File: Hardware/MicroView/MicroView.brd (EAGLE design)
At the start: 20.5 x 20.5 mm, 23 parts, among them J1 OLED_SCREEN, J2 MICROVIEW-16, J3 M03NS_SLIM, U1 MIC5205 3.3V, U2 SPX3819M5-L-5-0, U3 ATMEGA328P, Y1 16MHz

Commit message: Adding fids to both boards
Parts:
- added FID1, FID3: FIDUCIAL1X2, SparkFun-Aesthetics:FIDUCIAL-1X2
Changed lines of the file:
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@@
 <element name="LOGO1" library="SparkFun-Aesthetics" package="OSHW-LOGO-S" value="OSHW-LOGOS" x="-4.191" y="4.191"/>
 <element name="LOGO4" library="SparkFun-Aesthetics" package="SFE_LOGO_NAME_FLAME_.1" value="SFE_LOGO_NAME_FLAME.1_INCH" x="-8.128" y="0"/>
+<element name="FID1" library="SparkFun-Aesthetics" package="FIDUCIAL-1X2" value="FIDUCIAL1X2" x="7.62" y="9.525" rot="MR0"/>
+<element name="FID3" library="SparkFun-Aesthetics" package="FIDUCIAL-1X2" value="FIDUCIAL1X2" x="-5.08" y="-9.525" rot="MR0"/>
 </elements>
 <signals>

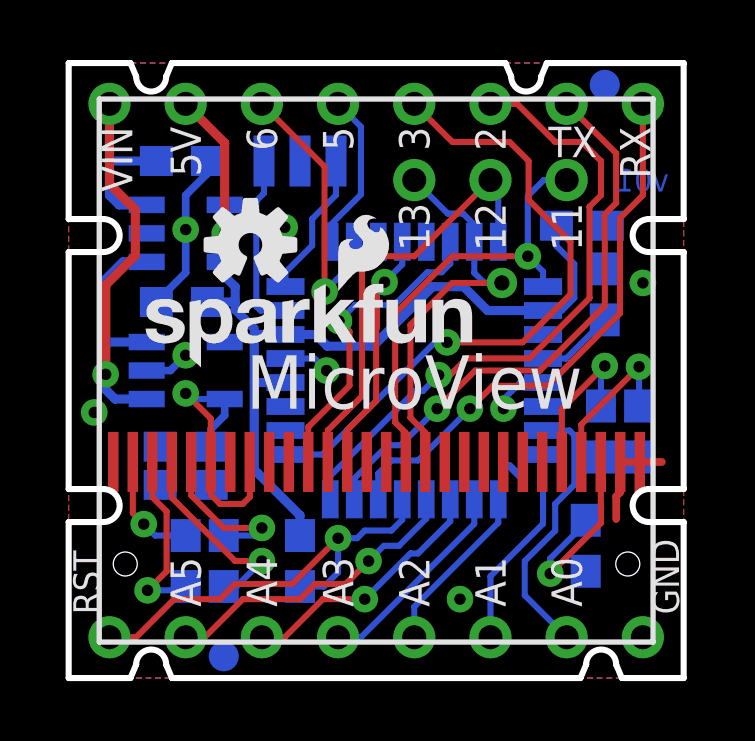
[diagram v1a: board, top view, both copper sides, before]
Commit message: Staggering/increasing drill on headers
Also spacing out resistors, increasing header fp on MicroViewUSB.
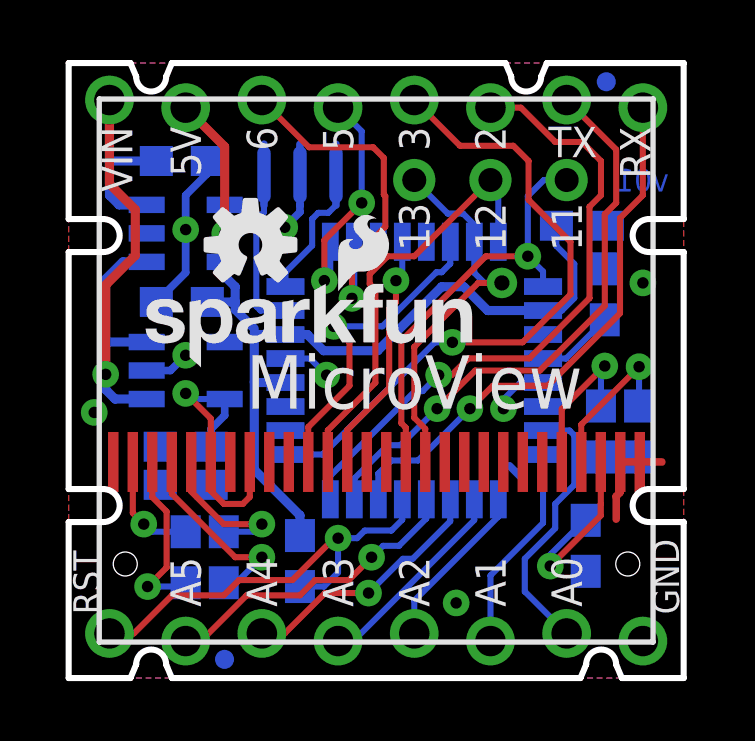
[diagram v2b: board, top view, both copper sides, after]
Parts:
- FID1, FID3: value FIDUCIAL1X2 -> FIDUCIALUFIDUCIAL; device SparkFun-Aesthetics:FIDUCIAL-1X2 -> SparkFun-Aesthetics:MICRO-FIDUCIAL
- moved Y1 0.46 mm to (-2.54, 6.53)
- moved C5 0.13 mm to (-6.35, -6.22)
- moved C6 0.13 mm to (-5.08, -6.22)
- moved FID1 0.11 mm to (7.67, 9.63)
- moved FID3 0.10 mm to (-5.05, -9.63)
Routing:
- net D6: track 9.19 -> 11.9 mm
- net D5: track 5.34 -> 7.98 mm, vias 0 -> 2
- net N$8: track 5.98 -> 4.51 mm
- net GND: track 14.4 -> 15.4 mm
- net D13/SCK: track 15.1 -> 14.2 mm
- net D11/MOSI: track 13.7 -> 13.1 mm

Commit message: Microview v02 -- new resistors and 3.3Vreg change
* Added pull-down resistor to OLED Reset. Also moved that pin to D7 on
the Arduino.
* Added pull-up resistor to D10/SS.
* Moved 3.3V regulator input to the 5V line (from Vin)
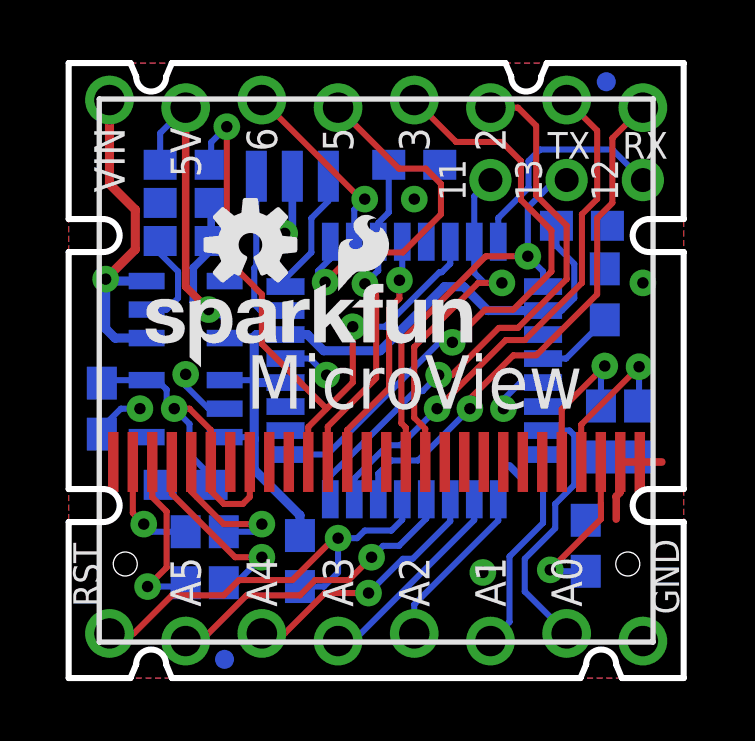
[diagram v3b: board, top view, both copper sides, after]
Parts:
- removed J3: M03NS_SLIM, microView-temp:1X03_NS_SLIM
- removed Y1: 16MHz, SparkFun-FreqCtrl:RESONATOR-SMD
- added J4: M03NS_SLIM, microView-temp:1X03_NS_SLIM
- added R3, R4: 10K, SparkFun-Resistors:0603-RES
- added Y2: RESONATORSMD, microView-temp:RESONATOR-SMD
- moved C2 3.78 mm to (-9.14, -1.27), turned to 270 degrees
- moved U2 2.54 mm to (-6.35, 2.03)
- moved C4 2.04 mm to (-6.35, 4.32)
- moved C1 1.40 mm to (-6.35, 5.59), turned to 0 degrees
- moved C3 1.27 mm to (-6.35, -3.81)
- moved U1 1.27 mm to (-6.35, -1.27), turned to 270 degrees
- turned C10 to 90 degrees
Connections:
- new net D7/!RESET!: OLED1.12, R4.2, U3.11
- net 5V: now also C1.1, R3.2, U1.1, U1.3
- net D10/SS: now also R3.1
- net D11/MOSI: now also J4.1; no longer J3.1
- net D12/MISO: now also J4.3; no longer J3.2, OLED1.12
- net D13/SCK: now also J4.2; no longer J3.3
- net GND: now also R4.1, Y2.2; no longer Y1.2
- net N$8: now also Y2.1; no longer Y1.1
- net N$9: now also Y2.3; no longer Y1.3
- net VIN: no longer C1.1, U1.1, U1.3
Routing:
- net VIN: track 25.6 -> 12.7 mm
- net D10/SS: track 10.8 -> 22.3 mm, vias 1 -> 2
- net D7/!RESET!: track 0.00 -> 11.1 mm, vias 0 -> 1
- net 5V: track 32.8 -> 41.1 mm
- net D12/MISO: track 14.5 -> 7.50 mm
- net D6: track 11.9 -> 6.36 mm
- net D5: track 7.98 -> 11.9 mm, vias 2 -> 1
- net D2: track 21.0 -> 18.7 mm
- net 3.3V: track 10.8 -> 12.4 mm
- net D3: track 21.4 -> 19.9 mm
- net TXD: track 19.1 -> 17.7 mm
- net N$8: track 4.51 -> 5.42 mm
- net D11/MOSI: track 13.1 -> 12.2 mm
- net GND: track 15.4 -> 16.2 mm
- net N$1: track 6.27 -> 5.50 mm
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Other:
- board text removed: "v01"

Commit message: Tying 3.3V reg enable to an ATmega pin (D4)
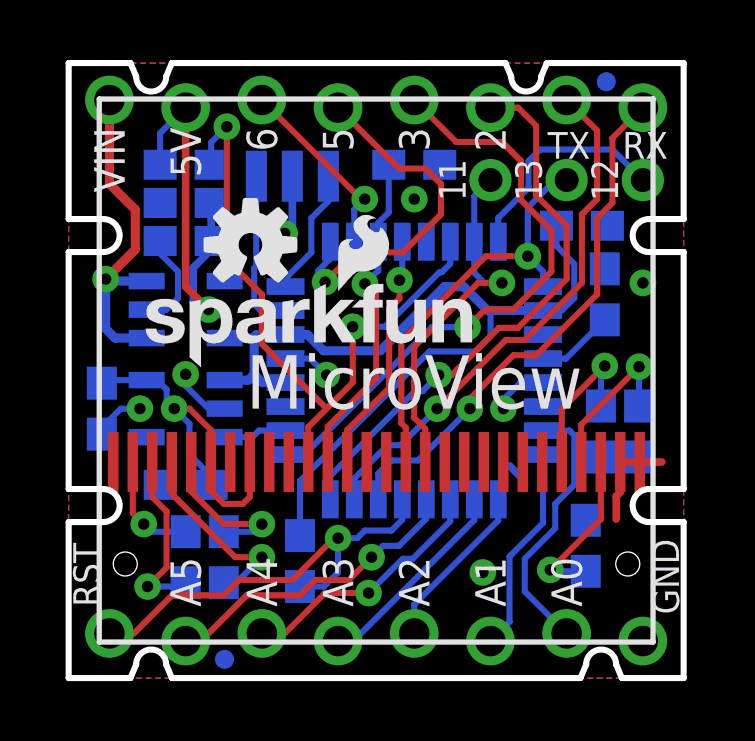
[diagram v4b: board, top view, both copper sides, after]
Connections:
- new net D4/3.3V_EN: U1.3, U3.2
- net 5V: no longer U1.3
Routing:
- net 5V: track 41.1 -> 45.3 mm
- net D4/3.3V_EN: track 0.00 -> 2.12 mm
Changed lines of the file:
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@@
 <layer number="50" name="dxf" color="7" fill="1" visible="no" active="no"/>
 <layer number="51" name="tDocu" color="6" fill="1" visible="yes" active="yes"/>
-<layer number="52" name="bDocu" color="7" fill="1" visible="yes" active="yes"/>
+<layer number="52" name="bDocu" color="7" fill="1" visible="no" active="yes"/>
 <layer number="53" name="tGND_GNDA" color="7" fill="9" visible="no" active="no"/>
 <layer number="54" name="bGND_GNDA" color="1" fill="9" visible="no" active="no"/>
@@
 <wire x1="5.5626" y1="2" x2="6.191" y2="2" width="0.2032" layer="16"/>
 <wire x1="6.191" y1="2" x2="6.604" y2="2.413" width="0.2032" layer="16"/>
-<wire x1="-2.54" y1="-5.5" x2="-2.54" y2="-4.826" width="0.3048" layer="16"/>
-<wire x1="-2.54" y1="-4.826" x2="-4.064" y2="-3.302" width="0.3048" layer="16"/>
-<wire x1="-4.064" y1="-3.302" x2="-4.064" y2="-2.286" width="0.3048" layer="16"/>
-<wire x1="-4.064" y1="-2.286" x2="-4.064" y2="-0.381" width="0.3048" layer="16"/>
 <wire x1="5.5626" y1="2" x2="3.715" y2="2" width="0.3048" layer="16"/>
 <wire x1="3.715" y1="2" x2="2.921" y2="2.794" width="0.3048" layer="16"/>
 <wire x1="-3.0226" y1="1.2" x2="-3.994" y2="1.2" width="0.3048" layer="16"/>
-<wire x1="-3.0226" y1="-0.4" x2="-4.045" y2="-0.4" width="0.3048" layer="16"/>
-<wire x1="-4.045" y1="-0.4" x2="-4.064" y2="-0.381" width="0.254" layer="16"/>
 <wire x1="2.921" y1="2.794" x2="2.2733" y2="2.794" width="0.3048" layer="16"/>
 <wire x1="-3.0226" y1="1.2" x2="-2.2922" y2="1.2" width="0.3048" layer="16"/>
@@
 <contactref element="U1" pad="1"/>
 <contactref element="C1" pad="1"/>
-<contactref element="U1" pad="3"/>
-<wire x1="-5.0499" y1="-0.32" x2="-4.125" y2="-0.32" width="0.2032" layer="16"/>
-<wire x1="-5.0499" y1="-2.22" x2="-4.13" y2="-2.22" width="0.2032" layer="16"/>
-<wire x1="-4.13" y1="-2.22" x2="-4.064" y2="-2.286" width="0.2032" layer="16"/>
 <wire x1="-5.0499" y1="1.082" x2="-4.112" y2="1.082" width="0.3048" layer="16"/>
 <wire x1="-4.112" y1="1.082" x2="-3.994" y2="1.2" width="0.3048" layer="16"/>
-<wire x1="-4.064" y1="-0.381" x2="-4.064" y2="1.034" width="0.3048" layer="16"/>
 <wire x1="-4.064" y1="1.034" x2="-4.112" y2="1.082" width="0.3048" layer="16"/>
-<wire x1="-4.064" y1="-0.381" x2="-4.125" y2="-0.32" width="0.254" layer="16"/>
 <wire x1="-5.5" y1="4.318" x2="-5.5" y2="4.025" width="0.254" layer="16"/>
 <wire x1="-5.5" y1="4.025" x2="-6.096" y2="3.429" width="0.254" layer="16"/>
@@
 <wire x1="-7.2" y1="6.858" x2="-7.2" y2="7.913" width="0.2032" layer="16"/>
 <wire x1="-7.2" y1="7.913" x2="-6.35" y2="8.763" width="0.2032" layer="16"/>
+<wire x1="-2.54" y1="-5.5" x2="-2.54" y2="-3.683" width="0.2032" layer="16"/>
+<wire x1="-2.54" y1="-3.683" x2="1.778" y2="0.635" width="0.2032" layer="16"/>
+<wire x1="1.778" y1="0.635" x2="3.302" y2="0.635" width="0.2032" layer="16"/>
+<wire x1="3.302" y1="0.635" x2="3.81" y2="1.143" width="0.2032" layer="16"/>
+<wire x1="3.81" y1="1.143" x2="3.81" y2="1.905" width="0.2032" layer="16"/>
+<wire x1="3.81" y1="1.905" x2="3.715" y2="2" width="0.2032" layer="16"/>
+<wire x1="-4.064" y1="1.034" x2="-4.064" y2="-0.127" width="0.3048" layer="16"/>
+<wire x1="-4.064" y1="-0.127" x2="-4.257" y2="-0.32" width="0.3048" layer="16"/>
+<wire x1="-5.0499" y1="-0.32" x2="-4.257" y2="-0.32" width="0.3048" layer="16"/>
+<wire x1="-3.0226" y1="-0.4" x2="-3.791" y2="-0.4" width="0.3048" layer="16"/>
+<wire x1="-3.791" y1="-0.4" x2="-4.064" y2="-0.127" width="0.3048" layer="16"/>
 </signal>
 <signal name="N$1">
@@
 <contactref element="U3" pad="1"/>
 <contactref element="J2" pad="12"/>
-<via x="2.54" y="0.9398" extent="1-16" drill="0.381"/>
+<via x="3.048" y="1.4478" extent="1-16" drill="0.381"/>
 <wire x1="4.826" y1="5.6896" x2="4.826" y2="6.985" width="0.2032" layer="1"/>
 <wire x1="4.826" y1="6.985" x2="4.191" y2="7.62" width="0.2032" layer="1"/>
 <wire x1="4.191" y1="7.62" x2="2.667" y2="7.62" width="0.2032" layer="1"/>
 <wire x1="2.667" y1="7.62" x2="1.27" y2="9.017" width="0.2032" layer="1"/>
-<wire x1="-3.0226" y1="-2.8" x2="-1.6316" y2="-2.8" width="0.2032" layer="16"/>
-<wire x1="-1.6316" y1="-2.8" x2="2.1082" y2="0.9398" width="0.2032" layer="16"/>
-<wire x1="2.54" y1="0.9398" x2="2.1082" y2="0.9398" width="0.2032" layer="16"/>
-<wire x1="2.54" y1="0.9398" x2="3.6322" y2="2.032" width="0.2032" layer="1"/>
+<wire x1="-3.0226" y1="-2.8" x2="-2.3936" y2="-2.8" width="0.2032" layer="16"/>
+<wire x1="-2.3936" y1="-2.8" x2="1.8542" y2="1.4478" width="0.2032" layer="16"/>
+<wire x1="3.048" y1="1.4478" x2="1.8542" y2="1.4478" width="0.2032" layer="16"/>
+<wire x1="3.048" y1="1.4478" x2="3.6322" y2="2.032" width="0.2032" layer="1"/>
 <wire x1="3.6322" y1="2.032" x2="4.572" y2="2.032" width="0.2032" layer="1"/>
 <wire x1="4.572" y1="2.032" x2="5.842" y2="3.302" width="0.2032" layer="1"/>
@@
 <wire x1="0.42" y1="6.858" x2="0.42" y2="5.2714" width="0.2032" layer="16"/>
 </signal>
+<signal name="D4/3.3V_EN">
+<contactref element="U1" pad="3"/>
+<contactref element="U3" pad="2"/>
+<wire x1="-3.0226" y1="-2" x2="-3.905" y2="-2" width="0.2032" layer="16"/>
+<wire x1="-3.905" y1="-2" x2="-4.125" y2="-2.22" width="0.2032" layer="16"/>
+<wire x1="-5.0499" y1="-2.22" x2="-4.125" y2="-2.22" width="0.2032" layer="16"/>
+</signal>
 </signals>

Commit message: Series resistors on MOSI and SCK (v03)
Limits current into OLED I/O lines. This in conjunction with some code
changes will help to protect the display from overvoltage.

This required removing pull-down resistor to RESET and pull-up to SS.
BUT! You can still program the display, using an ICSP, with the series
resistors on MOSI and SCK.
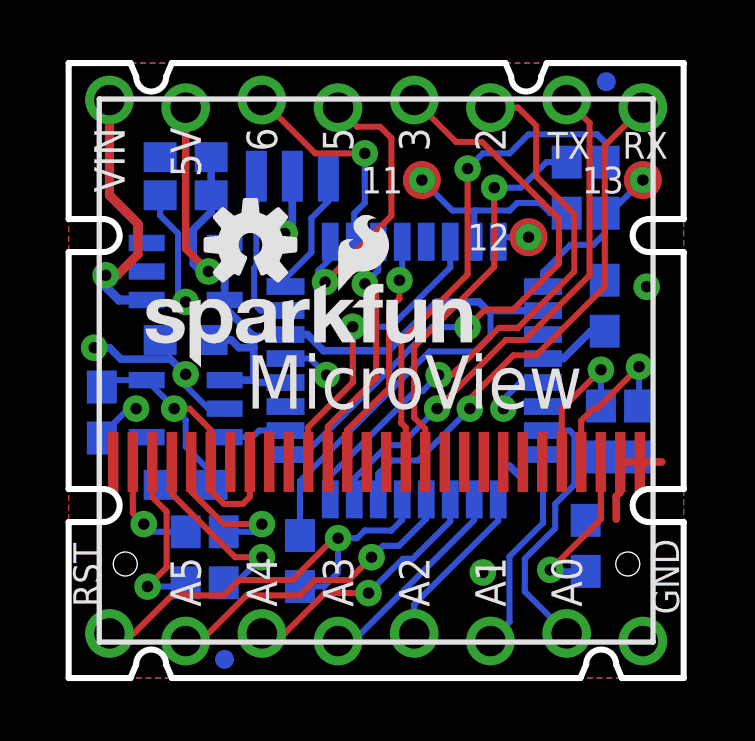
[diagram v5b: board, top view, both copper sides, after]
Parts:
- removed J4: M03NS_SLIM, microView-temp:1X03_NS_SLIM
- added TP1, TP2, TP3: (no value), SparkFun-Passives:PAD.03X.05
- R3, R4: value 10K -> 1k
- Y2: value RESONATORSMD -> 16MHz
- moved R3 14.0 mm to (7.62, 6.10), turned to 270 degrees
- moved C7 13.4 mm to (-6.35, 7.11), turned to 0 degrees
- moved R4 5.14 mm to (6.35, 6.10), turned to 270 degrees
- moved C1 4.57 mm to (-6.35, 1.02)
- moved C4 1.52 mm to (-6.35, 5.84)
- moved U2 1.27 mm to (-6.35, 3.30)
- moved C8 0.38 mm to (7.62, 2.16)
- moved C2 0.13 mm to (-9.14, -1.40)
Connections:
- new net D11: R4.2, TP3.P$1, U3.15
- new net D13: R3.2, TP2.P$1, U3.17
- net 5V: no longer R3.2
- net D10/SS: no longer R3.1
- net D11/MOSI: now also R4.1; no longer J4.1, U3.15
- net D12/MISO: now also TP1.P$1; no longer J4.3
- net D13/SCK: now also R3.1; no longer J4.2, U3.17
- net D7/!RESET!: no longer R4.2
- net GND: no longer R4.1
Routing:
- net D10/SS: track 22.3 -> 10.1 mm, vias 2 -> 1
- net D11: track 0.00 -> 6.55 mm, vias 0 -> 1
- net D12/MISO: track 7.50 -> 1.07 mm, vias 0 -> 1
- net D13: track 0.00 -> 5.47 mm, vias 0 -> 1
- net 5V: track 45.3 -> 39.9 mm
- net GND: track 16.2 -> 19.8 mm, vias 8 -> 9
- net D7/!RESET!: track 11.1 -> 8.35 mm
- net D13/SCK: track 14.0 -> 16.6 mm
- net D5: track 11.9 -> 9.52 mm
- net VIN: track 12.7 -> 14.3 mm
- net D11/MOSI: track 12.2 -> 13.2 mm
- net D6: track 6.36 -> 7.26 mm
- net C2N: track 5.94 -> 6.64 mm

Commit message: Moving some silk around. Production boards (v10).
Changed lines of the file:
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@@
 <plain>
 <text x="9.652" y="-8.128" size="0.889" layer="22" font="vector" ratio="15" rot="MR270" align="center-right">GND</text>
-<text x="5.842" y="-7.874" size="1.016" layer="22" font="vector" ratio="15" rot="MR270" align="center-right">A0</text>
+<text x="5.461" y="-7.366" size="1.016" layer="22" font="vector" ratio="15" rot="MR180" align="center">A0</text>
 <text x="3.81" y="-7.874" size="1.016" layer="22" font="vector" ratio="15" rot="MR270" align="center-right">A1</text>
 <text x="1.27" y="-7.874" size="1.016" layer="22" font="vector" ratio="15" rot="MR270" align="center-right">A2</text>
 <text x="-1.27" y="-7.874" size="1.016" layer="22" font="vector" ratio="15" rot="MR270" align="center-right">A3</text>
-<text x="-3.81" y="-7.874" size="1.016" layer="22" font="vector" ratio="15" rot="MR270" align="center-right">A4</text>
 <text x="-6.35" y="-7.874" size="1.016" layer="21" font="vector" ratio="15" rot="R270" align="center-right">A5</text>
-<text x="-9.652" y="-7.874" size="0.889" layer="22" font="vector" ratio="15" rot="MR270" align="center-right">RST</text>
-<text x="8.7884" y="7.9502" size="0.889" layer="22" font="vector" ratio="15" rot="MR0" align="top-center">RX</text>
-<text x="6.2484" y="7.9502" size="0.889" layer="22" font="vector" ratio="15" rot="MR0" align="top-center">TX</text>
-<text x="3.81" y="8.0264" size="0.889" layer="22" font="vector" ratio="15" rot="MR90" align="center-right">2</text>
-<text x="1.27" y="8.255" size="0.889" layer="22" font="vector" ratio="15" rot="MR90" align="center-right">3</text>
+<text x="-9.525" y="-7.874" size="0.889" layer="22" font="vector" ratio="15" rot="MR270" align="center-right">RST</text>
+<text x="8.7884" y="7.8232" size="0.889" layer="22" font="vector" ratio="15" rot="MR0" align="top-center">RX</text>
+<text x="3.81" y="8.001" size="0.889" layer="22" font="vector" ratio="15" rot="MR90" align="center-right">2</text>
+<text x="1.27" y="8.001" size="0.889" layer="22" font="vector" ratio="15" rot="MR90" align="center-right">3</text>
 <text x="-3.81" y="8.1026" size="1.016" layer="21" font="vector" ratio="15" rot="R270" align="center-left">6</text>
 <text x="-6.35" y="8.1026" size="1.016" layer="21" font="vector" ratio="15" rot="R270" align="center-left">5V</text>
-<text x="-8.89" y="8.255" size="0.889" layer="22" font="vector" ratio="15" rot="MR270" align="center-left">VIN</text>
-<text x="8.9662" y="7.9502" size="0.889" layer="21" font="vector" ratio="15" align="top-center">RX</text>
+<text x="-8.89" y="8.001" size="0.889" layer="22" font="vector" ratio="15" rot="MR270" align="center-left">VIN</text>
+<text x="8.4582" y="7.9502" size="0.889" layer="21" font="vector" ratio="15" align="top-center">RX</text>
 <text x="6.4262" y="7.9502" size="0.889" layer="21" font="vector" ratio="15" align="top-center">TX</text>
 <text x="3.81" y="8.1026" size="1.016" layer="21" font="vector" ratio="15" rot="R90" align="center-right">2</text>
 <text x="1.27" y="8.1026" size="1.016" layer="21" font="vector" ratio="15" rot="R90" align="center-right">3</text>
 <text x="-1.27" y="8.1026" size="1.016" layer="21" font="vector" ratio="15" rot="R90" align="center-right">5</text>
-<text x="-8.89" y="8.1026" size="1.016" layer="21" font="vector" ratio="15" rot="R90" align="center-right">VIN</text>
+<text x="-8.509" y="8.1026" size="1.016" layer="21" font="vector" ratio="15" rot="R90" align="center-right">VIN</text>
 <text x="9.652" y="-8.128" size="0.889" layer="21" font="vector" ratio="15" rot="R90" align="center-left">GND</text>
-<text x="6.35" y="-7.874" size="1.016" layer="21" font="vector" ratio="15" rot="R90" align="center-left">A0</text>
+<text x="6.858" y="-7.366" size="1.016" layer="21" font="vector" ratio="15" align="center">A0</text>
 <text x="3.81" y="-7.874" size="1.016" layer="21" font="vector" ratio="15" rot="R90" align="center-left">A1</text>
 <text x="1.27" y="-7.874" size="1.016" layer="21" font="vector" ratio="15" rot="R90" align="center-left">A2</text>
 <text x="-1.27" y="-7.874" size="1.016" layer="21" font="vector" ratio="15" rot="R90" align="center-left">A3</text>
-<text x="-3.81" y="-7.874" size="1.016" layer="21" font="vector" ratio="15" rot="R90" align="center-left">A4</text>
+<text x="-3.683" y="-7.366" size="1.016" layer="21" font="vector" ratio="15" align="center">A4</text>
 <text x="-9.652" y="-7.874" size="0.889" layer="21" font="vector" ratio="15" rot="R90" align="center-left">RST</text>
 <wire x1="-10.25" y1="-10.25" x2="-10.25" y2="-5.05" width="0.2032" layer="20"/>
@@
 <text x="7.62" y="-20.32" size="1.778" layer="51" ratio="15">Jim Lindblom, JP Liew, Marcus Schappi</text>
 <text x="1.27" y="-0.381" size="1.778" layer="21" font="vector" ratio="15" align="center">MicroView</text>
-<text x="8.255" y="6.35" size="0.889" layer="21" font="vector" ratio="15" align="center-right">13</text>
-<text x="4.445" y="4.445" size="0.889" layer="21" font="vector" ratio="15" align="center-right">12</text>
-<text x="0.889" y="6.35" size="0.889" layer="21" font="vector" ratio="15" align="center-right">11</text>
+<text x="8.382" y="6.35" size="0.889" layer="21" font="vector" ratio="15" align="center-right">13</text>
+<text x="4.572" y="4.445" size="0.889" layer="21" font="vector" ratio="15" align="center-right">12</text>
+<text x="1.016" y="6.35" size="0.889" layer="21" font="vector" ratio="15" align="center-right">11</text>
 </plain>
 <attributes>
@@
 <wire x1="-3.0226" y1="0.4" x2="-2.2034" y2="0.4" width="0.2032" layer="16"/>
 <wire x1="-2.2034" y1="0.4" x2="-1.651" y2="-0.1524" width="0.2032" layer="16"/>
-<via x="3.556" y="-6.731" extent="1-16" drill="0.381"/>
+<via x="2.794" y="-7.62" extent="1-16" drill="0.381"/>
 <wire x1="4.826" y1="-3.556" x2="4.445" y2="-3.175" width="0.254" layer="16"/>
 <wire x1="8.128" y1="-3.048" x2="8.128" y2="-4.064" width="0.254" layer="1"/>
